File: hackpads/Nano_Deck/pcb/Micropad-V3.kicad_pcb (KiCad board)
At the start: 2 copper layers, 78.9 x 91.5 mm, 51 parts, among them J1 OLED_128x64, SW1 RotaryEncoder_Switch, SW2 RotaryEncoder_Switch, U1 MCU_Seeed_XIAO_RP2040, U2 PCF8574A

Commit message: updated pcb
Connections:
- U1 pad 7: Row -1 -> RGB
- U2 pad 4: Row 0 -> Row -1
- U2 pad 5: Row 1 -> Row 0
- U2 pad 6: Row 2 -> Row 1
- U2 pad 7: Row 3 -> Row 2
- U2 pad 9: RGB -> Row 3
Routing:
- net RGB: track 30.5 -> 48.3 mm, vias 4 -> 6
- net Row -1: track 181.5 -> 197.5 mm, vias 0 -> 2
- net Row 3: track 150.5 -> 164.4 mm
- net Row 1: track 72.8 -> 75.3 mm
- net Row 0: vias 0 -> 2
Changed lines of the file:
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@@
 		)
 		(sheetname "Root")
-		(sheetfile "Micropad-V2.kicad_sch")
+		(sheetfile "Micropad-V3.kicad_sch")
 		(attr through_hole)
 		(fp_line
@@
 			(layers "B.Cu" "B.Paste" "B.Mask")
 			(roundrect_rratio 0.25)
-			(net 4 "Row -1")
+			(net 2 "RGB")
 			(pinfunction "PB08_A6_D6_TX")
 			(pintype "passive")
@@
 			(layers "*.Cu" "*.Mask")
 			(remove_unused_layers no)
-			(net 4 "Row -1")
+			(net 2 "RGB")
 			(pinfunction "PB08_A6_D6_TX")
 			(pintype "passive")
@@
 			(layers "*.Cu" "*.Mask")
 			(remove_unused_layers no)
-			(net 5 "Row 0")
+			(net 4 "Row -1")
 			(pinfunction "P0")
 			(pintype "bidirectional")
@@
 			(layers "*.Cu" "*.Mask")
 			(remove_unused_layers no)
-			(net 7 "Row 1")
+			(net 5 "Row 0")
 			(pinfunction "P1")
 			(pintype "bidirectional")
@@
 			(layers "*.Cu" "*.Mask")
 			(remove_unused_layers no)
-			(net 10 "Row 2")
+			(net 7 "Row 1")
 			(pinfunction "P2")
 			(pintype "bidirectional")
@@
 			(layers "*.Cu" "*.Mask")
 			(remove_unused_layers no)
-			(net 11 "Row 3")
+			(net 10 "Row 2")
 			(pinfunction "P3")
 			(pintype "bidirectional")
@@
 			(layers "*.Cu" "*.Mask")
 			(remove_unused_layers no)
-			(net 2 "RGB")
+			(net 11 "Row 3")
 			(pinfunction "P4")
 			(pintype "bidirectional")
@@
 	)
 	(segment
+		(start 115.74 74.76)
+		(end 117.22 74.76)
+		(width 0.2)
+		(layer "F.Cu")
+		(net 2)
+	)
+	(segment
+		(start 99.32 76.36)
+		(end 101.43375 74.24625)
+		(width 0.2)
+		(layer "F.Cu")
+		(net 2)
+	)
+	(segment
 		(start 82.855664 60.824336)
 		(end 87.072814 60.824336)
@@
 	)
 	(segment
+		(start 102.68625 74.24625)
+		(end 103.64 75.2)
+		(width 0.2)
+		(layer "F.Cu")
+		(net 2)
+	)
+	(segment
 		(start 87.072814 60.824336)
 		(end 88.43894 62.190462)
@@
 	)
 	(segment
-		(start 99.32 76.36)
-		(end 101.32 76.36)
+		(start 101.43375 74.24625)
+		(end 102.68625 74.24625)
 		(width 0.2)
 		(layer "F.Cu")
@@
 	)
 	(via
+		(at 117.22 74.76)
+		(size 0.6)
+		(drill 0.3)
+		(layers "F.Cu" "B.Cu")
+		(net 2)
+	)
+	(via
+		(at 103.64 75.2)
+		(size 0.6)
+		(drill 0.3)
+		(layers "F.Cu" "B.Cu")
+		(net 2)
+	)
+	(via
 		(at 88.43894 63.424426)
 		(size 0.6)
@@
 	)
 	(via
-		(at 82.855664 60.824336)
+		(at 115.74 74.76)
 		(size 0.6)
 		(drill 0.3)
@@
 	)
 	(via
-		(at 101.32 76.36)
+		(at 82.855664 60.824336)
 		(size 0.6)
 		(drill 0.3)
@@
 	)
 	(segment
+		(start 117.22 74.76)
+		(end 117.22 73.01)
+		(width 0.2)
+		(layer "B.Cu")
+		(net 2)
+	)
+	(segment
+		(start 117.22 73.01)
+		(end 116.84 72.63)
+		(width 0.2)
+		(layer "B.Cu")
+		(net 2)
+	)
+	(segment
 		(start 90.549426 63.424426)
 		(end 99.32 72.195)
@@
 	)
 	(segment
-		(start 101.32 76.8483)
-		(end 100.33 77.8383)
+		(start 115.3 75.2)
+		(end 115.74 74.76)
 		(width 0.2)
 		(layer "B.Cu")
@@
 	)
 	(segment
-		(start 82.82 61.36)
-		(end 82.82 60.86)
+		(start 103.64 75.2)
+		(end 115.3 75.2)
 		(width 0.2)
 		(layer "B.Cu")
@@
 	)
 	(segment
-		(start 101.32 76.36)
-		(end 101.32 76.8483)
+		(start 82.82 61.36)
+		(end 82.82 60.86)
 		(width 0.2)
 		(layer "B.Cu")
@@
 	)
 	(segment
+		(start 111.81 84.1383)
+		(end 110.49 85.4583)
+		(width 0.2)
+		(layer "F.Cu")
+		(net 4)
+	)
+	(segment
+		(start 116.283985 80.23)
+		(end 112.413985 84.1)
+		(width 0.2)
+		(layer "F.Cu")
+		(net 4)
+	)
+	(segment
 		(start 81.801522 73.73)
 		(end 70.92 62.848478)
@@
 	)
 	(segment
+		(start 123.0375 72.63)
+		(end 123.0375 78.7625)
+		(width 0.2)
+		(layer "F.Cu")
+		(net 4)
+	)
+	(segment
 		(start 70.92 56.244315)
 		(end 71.154315 56.01)
@@
 	)
 	(segment
-		(start 116.84 72.63)
-		(end 123.0375 72.63)
+		(start 111.81 84.1)
+		(end 111.81 84.1383)
+		(width 0.2)
+		(layer "F.Cu")
+		(net 4)
+	)
+	(segment
+		(start 122.77 80.23)
+		(end 116.283985 80.23)
 		(width 0.2)
 		(layer "F.Cu")
@@
 	)
 	(segment
+		(start 112.413985 84.1)
+		(end 111.81 84.1)
+		(width 0.2)
+		(layer "F.Cu")
+		(net 4)
+	)
+	(segment
 		(start 103.98375 71.801885)
 		(end 102.055635 73.73)
@@
 	)
 	(segment
-		(start 136.74 79.24)
-		(end 146.93 79.24)
+		(start 123.0375 78.7625)
+		(end 122.77 79.03)
 		(width 0.2)
 		(layer "F.Cu")
-		(net 5)
+		(net 4)
+	)
+	(via
+		(at 122.77 80.23)
+		(size 0.6)
+		(drill 0.3)
+		(layers "F.Cu" "B.Cu")
+		(net 4)
+	)
+	(via
+		(at 122.77 79.03)
+		(size 0.6)
+		(drill 0.3)
+		(layers "F.Cu" "B.Cu")
+		(net 4)
 	)
 	(segment
-		(start 110.49 81.578049)
-		(end 110.49 85.4583)
+		(start 122.77 79.03)
+		(end 122.77 80.23)
+		(width 0.2)
+		(layer "B.Cu")
+		(net 4)
+	)
+	(segment
+		(start 136.74 79.24)
+		(end 146.93 79.24)
 		(width 0.2)
 		(layer "F.Cu")
@@
 	)
 	(segment
+		(start 107.035362 84.543662)
+		(end 107.667157 85.175457)
+		(width 0.2)
+		(layer "F.Cu")
+		(net 5)
+	)
+	(segment
+		(start 108.541951 79.63)
+		(end 108.541951 82.218049)
+		(width 0.2)
+		(layer "F.Cu")
+		(net 5)
+	)
+	(segment
 		(start 90.17 79.63)
 		(end 136.35 79.63)
@@
 	)
 	(segment
-		(start 108.541951 79.63)
-		(end 110.49 81.578049)
+		(start 108.541951 82.218049)
+		(end 107.8 82.96)
 		(width 0.2)
 		(layer "F.Cu")
@@
 	)
 	(segment
+		(start 106.87 84.543662)
+		(end 107.035362 84.543662)
+		(width 0.2)
+		(layer "F.Cu")
+		(net 5)
+	)
+	(via
+		(at 106.87 84.543662)
+		(size 0.6)
+		(drill 0.3)
+		(layers "F.Cu" "B.Cu")
+		(net 5)
+	)
+	(via
+		(at 107.8 82.96)
+		(size 0.6)
+		(drill 0.3)
+		(layers "F.Cu" "B.Cu")
+		(net 5)
+	)
+	(segment
+		(start 107.8 82.96)
+		(end 107.8 83.613662)
+		(width 0.2)
+		(layer "B.Cu")
+		(net 5)
+	)
+	(segment
+		(start 107.8 83.613662)
+		(end 106.87 84.543662)
+		(width 0.2)
+		(layer "B.Cu")
+		(net 5)
+	)
+	(segment
 		(start 83.185 71.755)
 		(end 89.915 71.755)
@@
 	)
 	(segment
+		(start 107.78 87.8283)
+		(end 110.32 87.8283)
+		(width 0.2)
+		(layer "F.Cu")
+		(net 7)
+	)
+	(segment
 		(start 116.68 98.68)
 		(end 101.17 98.68)
@@
 	)
 	(segment
-		(start 110.32 87.8283)
-		(end 107.95 85.4583)
+		(start 147.32 98.68)
+		(end 139.79 98.68)
 		(width 0.2)
 		(layer "F.Cu")
@@
 	)
 	(segment
-		(start 147.32 98.68)
-		(end 139.79 98.68)
+		(start 98.138428 98.321572)
+		(end 97.78 98.68)
 		(width 0.2)
 		(layer "F.Cu")
@@
 	)
 	(segment
-		(start 98.138428 98.321572)
-		(end 97.78 98.68)
+		(start 105.41 85.4583)
+		(end 107.78 87.8283)
 		(width 0.2)
 		(layer "F.Cu")
@@
 	)
 	(segment
-		(start 104.4208 86.4475)
-		(end 105.41 85.4583)
-		(width 0.2)
-		(layer "F.Cu")
-		(net 10)
-	)
-	(segment
 		(start 114.782588 117.48)
 		(end 114.630088 117.6325)
@@
 	)
 	(segment
+		(start 103.4316 85.4583)
+		(end 103.27 85.4583)
+		(width 0.2)
+		(layer "F.Cu")
+		(net 10)
+	)
+	(segment
 		(start 147.07 117.48)
 		(end 114.782588 117.48)
@@
 	)
 	(segment
+		(start 104.4208 86.4475)
+		(end 103.4316 85.4583)
+		(width 0.2)
+		(layer "F.Cu")
+		(net 10)
+	)
+	(segment
 		(start 110.32 102.56)
 		(end 89.07 102.56)
@@
 	)
 	(segment
+		(start 89.196015 77.8383)
+		(end 100.33 77.8383)
+		(width 0.2)
+		(layer "F.Cu")
+		(net 11)
+	)
+	(segment
 		(start 103.775625 118.435625)
 		(end 103.38 118.04)
@@
 	)
 	(segment
+		(start 88.67 95.778049)
+		(end 93.242157 91.205892)
+		(width 0.2)
+		(layer "F.Cu")
+		(net 11)
+	)
+	(segment
+		(start 88.67 86.633735)
+		(end 88.67 78.364315)
+		(width 0.2)
+		(layer "F.Cu")
+		(net 11)
+	)
+	(segment
 		(start 102.3175 136.38)
 		(end 102.6775 136.74)
@@
 	)
 	(segment
-		(start 88.67 95.778049)
-		(end 99.937449 84.5106)
+		(start 93.242157 91.205892)
+		(end 88.67 86.633735)
 		(width 0.2)
 		(layer "F.Cu")
@@
 	)
 	(segment
-		(start 101.9223 84.5106)
-		(end 102.87 85.4583)
-		(width 0.2)
-		(layer "F.Cu")
-		(net 11)
-	)
-	(segment
-		(start 99.937449 84.5106)
-		(end 101.9223 84.5106)
+		(start 88.67 78.364315)
+		(end 89.196015 77.8383)
 		(width 0.2)
 		(layer "F.Cu")

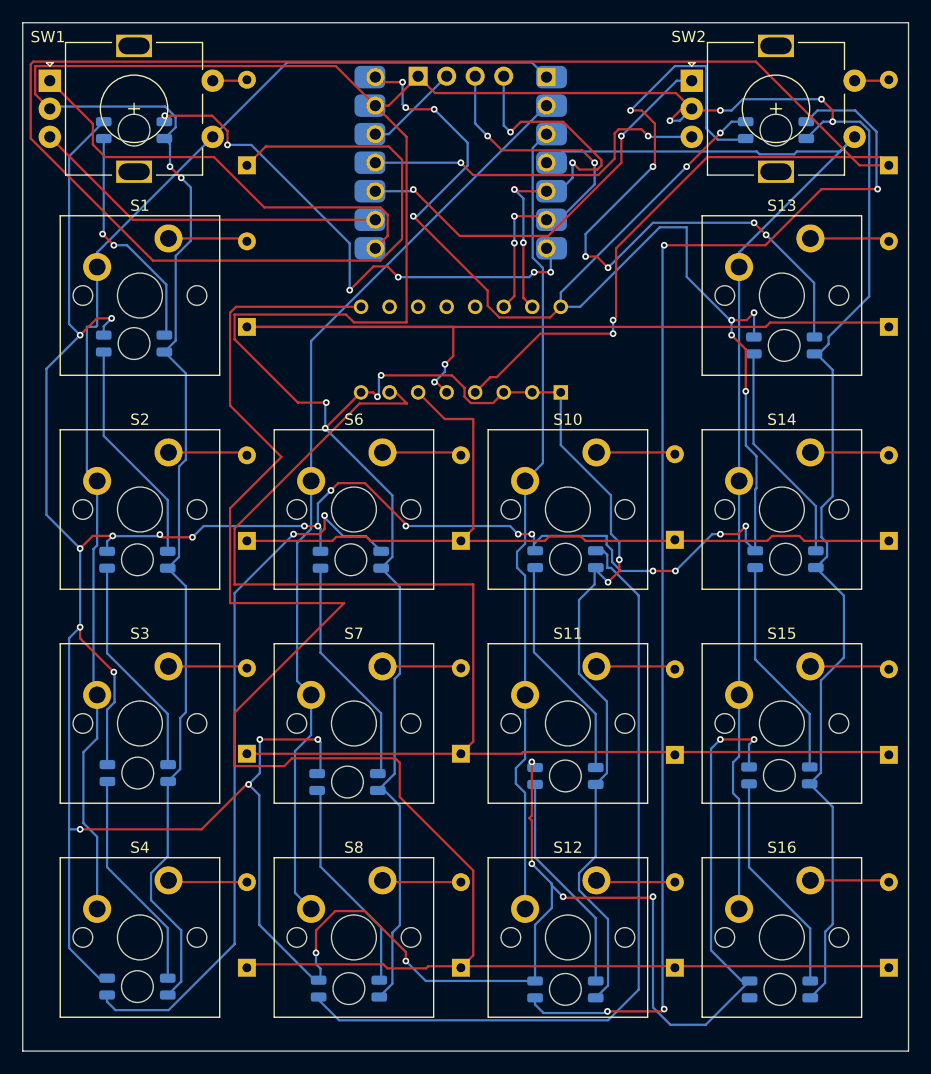
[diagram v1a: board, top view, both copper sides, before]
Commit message: added resistors for 12c
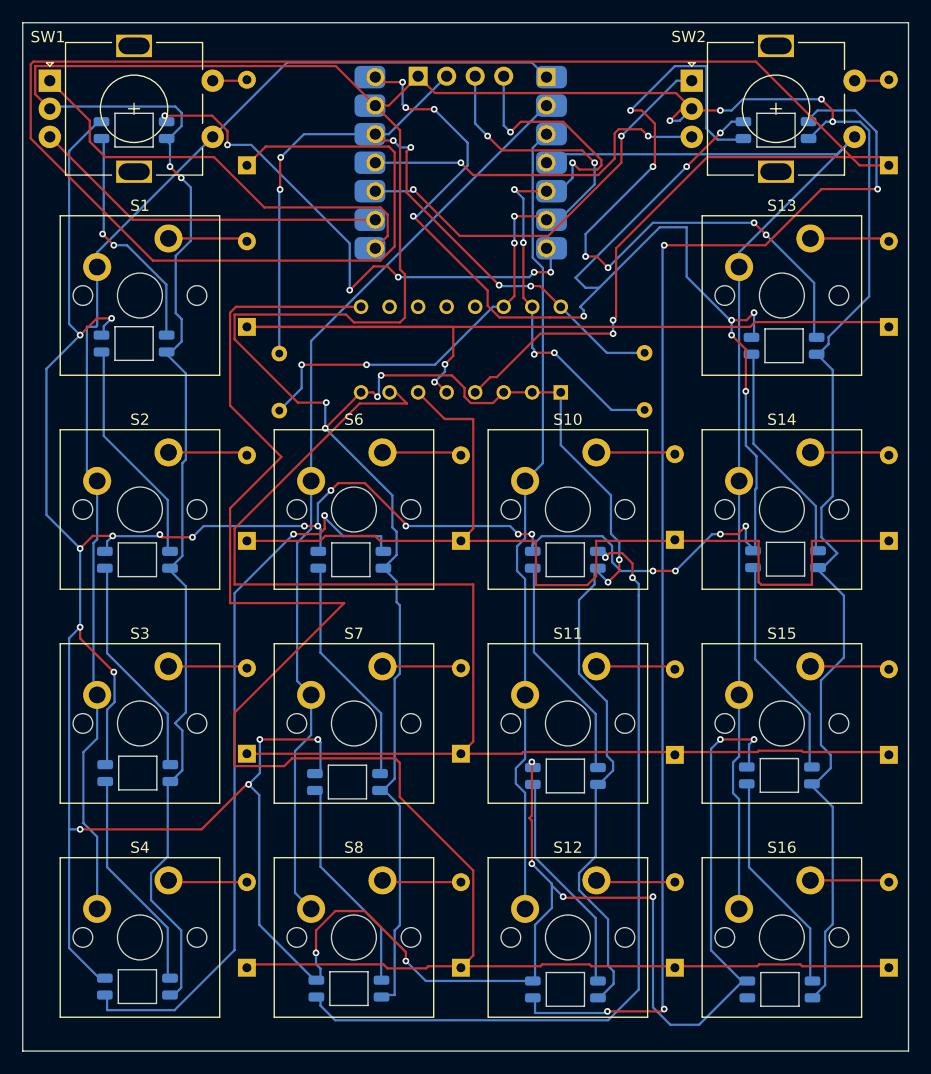
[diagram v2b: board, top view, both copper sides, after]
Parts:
- added R1: Resistor, Resistor_THT:R_Axial_DIN0204_L3.6mm_D1.6mm_P5.08mm_Horizontal, B.Cu at (93.0, 87.1)
- added R2: Resistor, Resistor_THT:R_Axial_DIN0204_L3.6mm_D1.6mm_P5.08mm_Horizontal, B.Cu at (125.6, 81.9)
- moved D25 0.05 mm to (118.5, 100.4)
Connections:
- U2 pad 16: +5V -> +3V3
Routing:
- net +3V3: track 8.49 -> 70.4 mm, vias 0 -> 6
- net Net-(J1-SCL): track 35.3 -> 60.3 mm, vias 4 -> 6
- net Net-(J1-SDA): track 36.7 -> 53.0 mm, vias 4 -> 6
- net Row 1: track 75.3 -> 89.8 mm
- net GND: track 470.9 -> 475.1 mm
- net Net-(D24-DOUT): track 72.1 -> 73.7 mm, vias 0 -> 2
- net Net-(D21-DOUT): track 64.0 -> 65.5 mm
- net +5V: track 451.4 -> 450.6 mm, vias 40 -> 41
- net Row -1: track 197.5 -> 196.9 mm
